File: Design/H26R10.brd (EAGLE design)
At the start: 34.6 x 60 mm, 66 parts, among them P1 HEXABIT_17.32_X2_NO_P5_P10_P1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, U1 STM32F091RBT6STMICROELECTRONI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, U2 AD8275BRMZ, U3 ADR431ARMZ, U4 AD8295BCPZ-WP, U5 AD7687BRMZ, X1 XTALL_CSTCE8M00G52, X2 1751251, X3 CON-PHOENIX-350_1751277

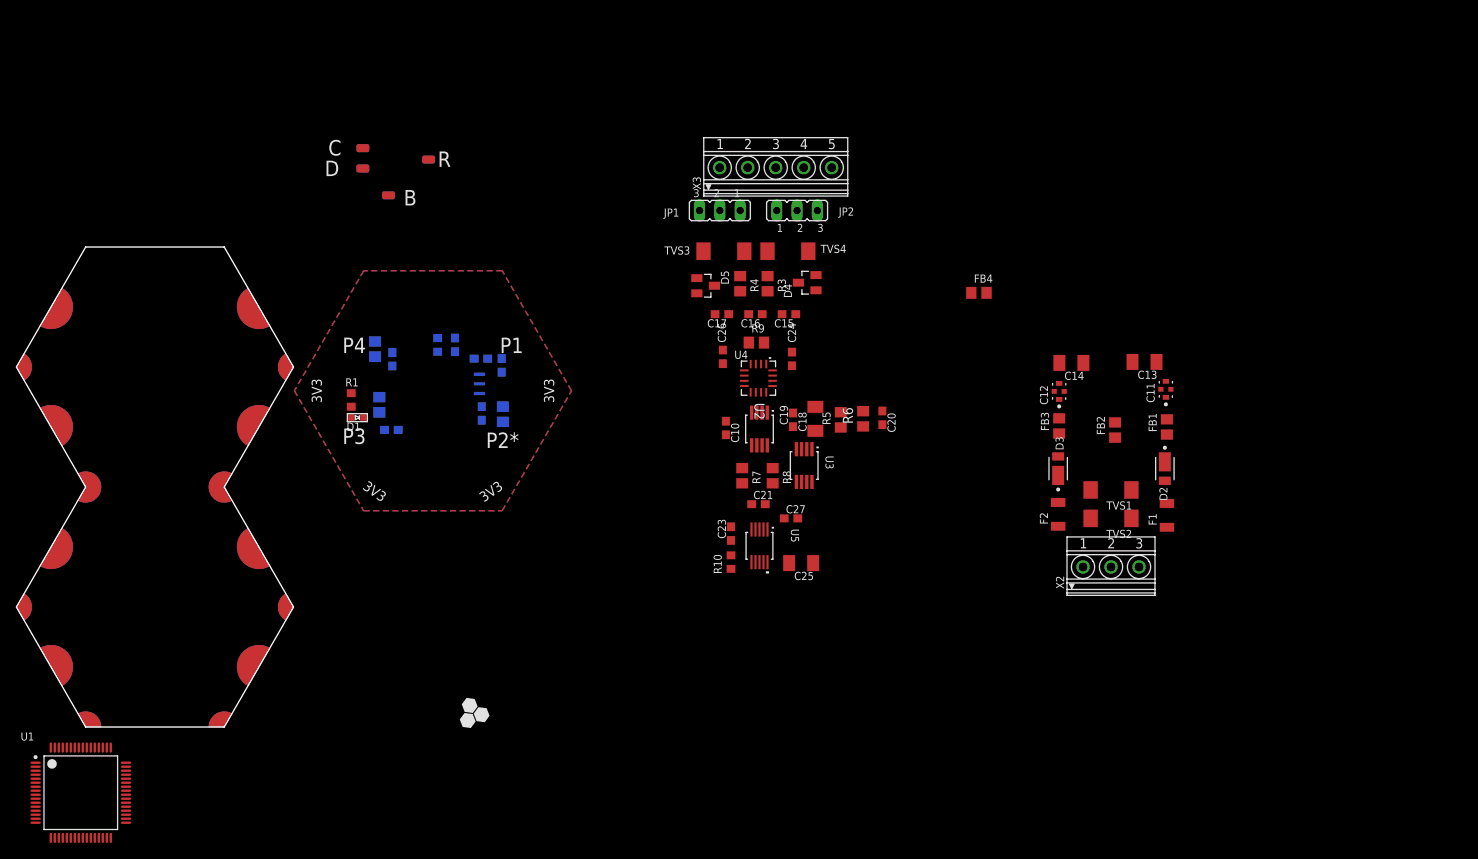
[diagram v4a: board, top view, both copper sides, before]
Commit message: Rearrange uart connections Route analog section
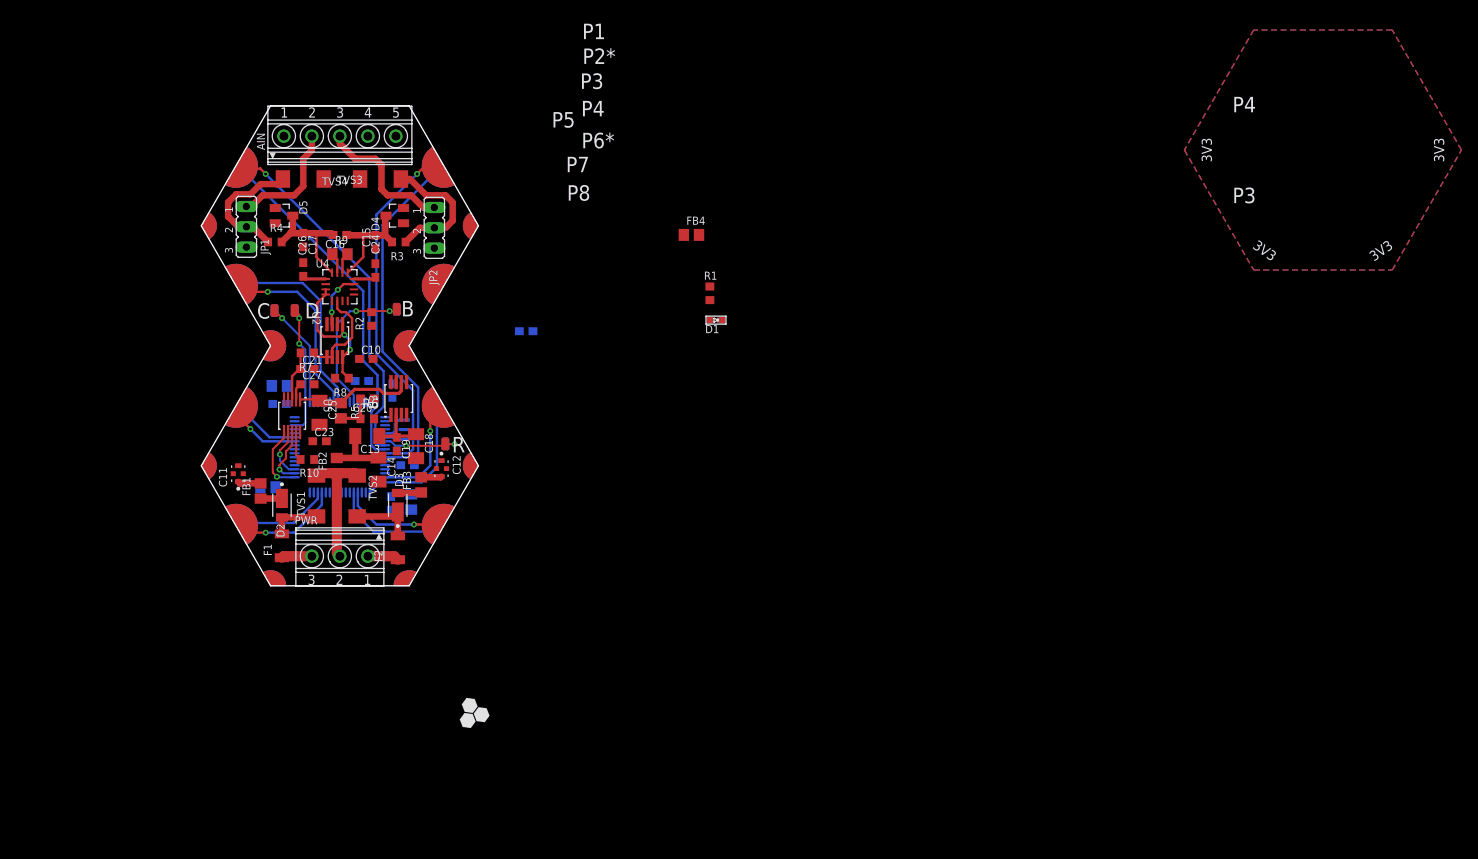
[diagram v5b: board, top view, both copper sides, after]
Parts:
- removed X2: 1751251, con-phoenix-350:1751251
- removed X3: CON-PHOENIX-350_1751277, Hexabitz:CON-PHOENIX-350_1751277
- added AIN: CON-PHOENIX-350_1751277, Hexabitz:CON-PHOENIX-350_1751277
- added PWR: 1751251, con-phoenix-350:1751251
- R3, R4, R6, R7, R8: device Hexabitz:R-0805 -> Hexabitz:R-0603
- moved C11 116.4 mm to (10.3, 24.3)
- moved FB1 113.6 mm to (13.1, 22.1)
- moved F1 110.7 mm to (15.7, 15.2)
- moved D2 110.5 mm to (15.7, 20.3)
- moved TVS1 99.3 mm to (20.1, 21.5), turned to 90 degrees
- moved C13 97.6 mm to (26.4, 29.0)
- moved FB2 97.4 mm to (22.6, 25.3)
- moved TVS2 94.3 mm to (25.1, 21.5), turned to 270 degrees
- moved C14 87.6 mm to (27.8, 24.8), turned to 270 degrees
- moved D3 82.7 mm to (30.2, 20.3)
- moved F2 82.7 mm to (30.2, 15.0)
- moved FB3 80.1 mm to (33.1, 22.9)
- moved C12 77.8 mm to (35.7, 24.9), turned to 270 degrees
- moved C20 64.4 mm to (26.4, 33.7), turned to 180 degrees
- moved C25 63.1 mm to (20.4, 31.9), turned to 270 degrees
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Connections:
- net +5V renamed +2.5V
- removed net N$29: P1.PAD_PU1
- removed net N$30: P1.PAD_PU2
- removed net N$34: P1.PAD_PD1, P1.PAD_PD2, P1.PAD_PD3, P1.PAD_PD4, P1.PAD_PD6, P1.PAD_PD7, P1.PAD_PD8, P1.PAD_PD9, P1.PAD_PU3, P1.PAD_PU4, P1.PAD_PU6, P1.PAD_PU7, P1.PAD_PU8, P1.PAD_PU9
- removed net UART1_RX: U1.43
- removed net UART1_TX: U1.42
- new net UART1_RX*: P1.PAD_PD7, U1.43
- new net UART1_TX*: P1.PAD_PU7, U1.42
- net +15V: now also AIN.5; no longer X3.5
- net -15V: now also AIN.4; no longer X3.4
- net AGND: now also AIN.1; no longer X3.1
- net N$1: now also AIN.3; no longer X3.3
- net N$15: now also PWR.3; no longer X2.3
- net N$16: now also PWR.1; no longer X2.1
- net N$19: now also PWR.2; no longer X2.2
- net N$2: now also AIN.2; no longer X3.2
- net UART2_RX*: now also P1.PAD_PD3
- net UART2_TX*: now also P1.PAD_PU3
- net UART3_RX: now also P1.PAD_PD6
- net UART3_TX: now also P1.PAD_PU6
- net UART4_RX: now also P1.PAD_PD2
- net UART4_TX: now also P1.PAD_PU2
- net UART5_RX: now also P1.PAD_PD8
- net UART5_TX: now also P1.PAD_PU8
- net UART6_RX: now also P1.PAD_PD4
- net UART6_TX: now also P1.PAD_PU4
- net UART7_RX: now also P1.PAD_PD9
- net UART7_TX: now also P1.PAD_PU9
- net UART8_RX: now also P1.PAD_PD1
- net UART8_TX: now also P1.PAD_PU1
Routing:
- net UART8_TX: track 0.00 -> 45.1 mm, vias 0 -> 1
- net UART7_TX: track 0.00 -> 44.9 mm, vias 0 -> 1
- net UART8_RX: track 0.00 -> 44.6 mm
- net UART7_RX: track 0.00 -> 43.9 mm
- net UART5_RX: track 0.00 -> 24.4 mm
- net UART5_TX: track 0.00 -> 23.2 mm, vias 0 -> 1
- net B1: track 0.00 -> 19.9 mm, vias 0 -> 2
- net N$1: track 0.00 -> 17.8 mm
- net N$7: track 0.00 -> 17.2 mm, vias 0 -> 2
- net UART2_RX*: track 0.00 -> 17.1 mm
- net AD8295_A1O: track 0.00 -> 17.1 mm, vias 0 -> 2
- net N$8: track 0.00 -> 16.9 mm
- net N$10: track 0.00 -> 16.1 mm
- net N$19: track 0.00 -> 15.9 mm
- net N$12: track 0.00 -> 15.0 mm
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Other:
- board text added: "P5"
- board text added: "P6*"
- board text added: "P7"
- board text added: "P8"

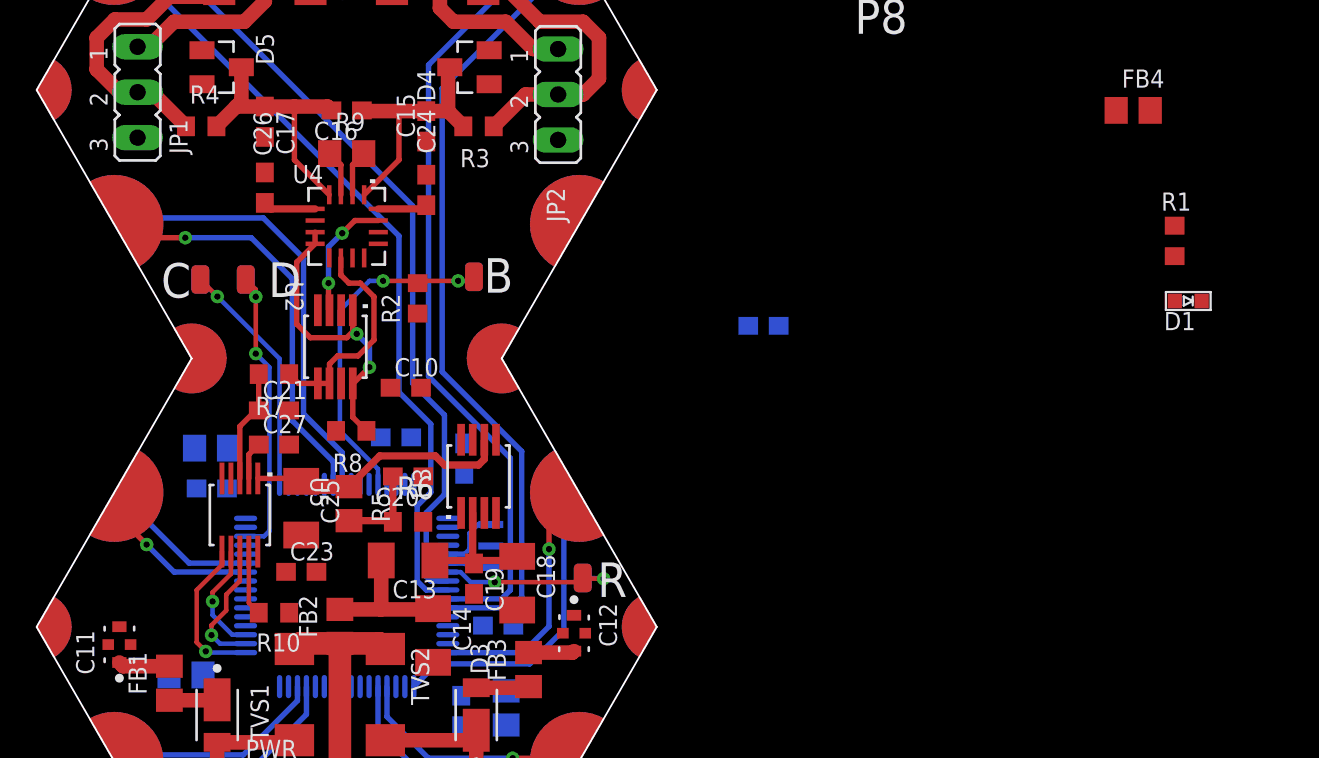
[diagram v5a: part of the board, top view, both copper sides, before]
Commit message: More routing Add 2 more layers Add layer stack note
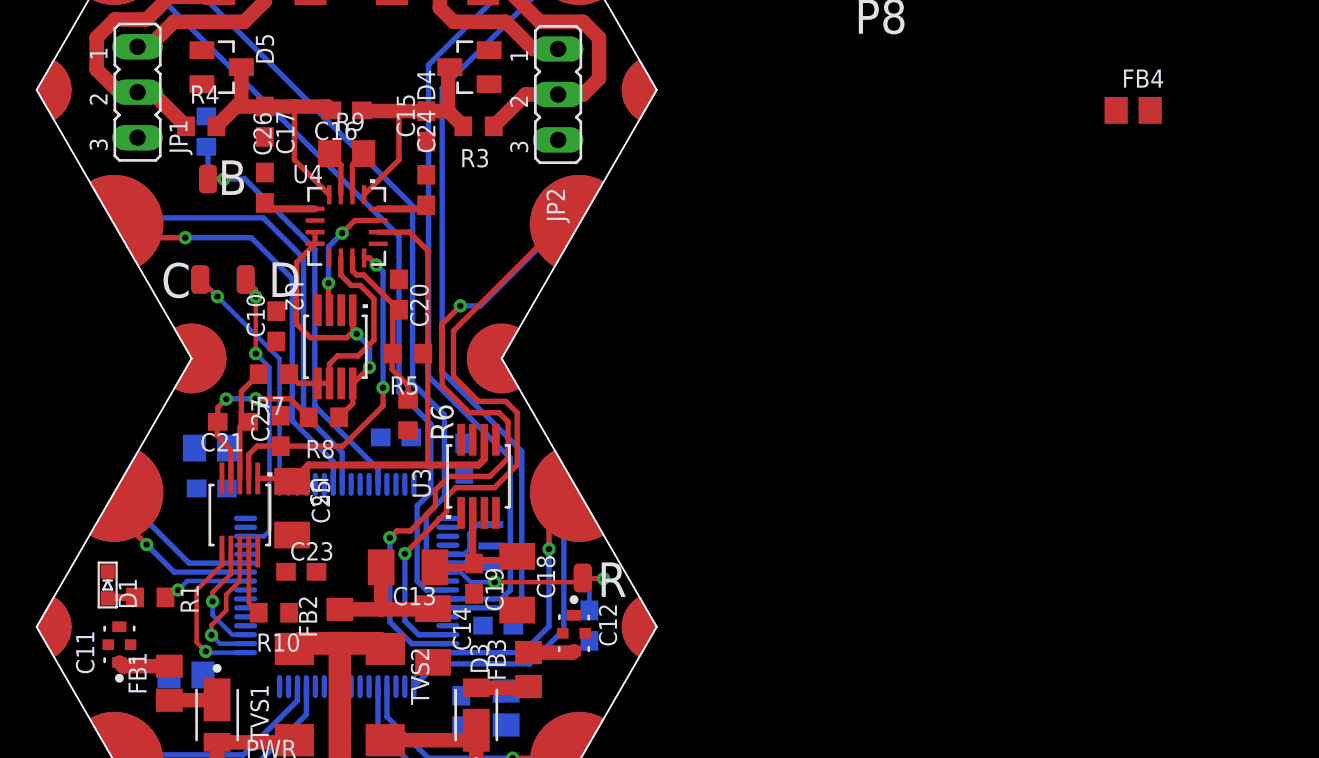
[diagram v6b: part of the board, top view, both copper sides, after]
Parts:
- R5: device Hexabitz:R-0805 -> Hexabitz:R-0603
- moved D1 62.4 mm to (9.63, 27.6), turned to 180 degrees
- moved R1 60.6 mm to (12.0, 26.9), turned to 0 degrees
- moved C8 19.4 mm to (36.5, 25.3), turned to 270 degrees
- moved B 15.8 mm to (15.2, 50.3)
- moved R2 15.0 mm to (15.1, 52.9), flipped to the bottom, turned to 270 degrees
- moved C20 10.2 mm to (25.9, 43.8), turned to 270 degrees
- moved R5 9.01 mm to (26.4, 40.5), turned to 180 degrees
- moved C10 8.01 mm to (19.1, 42.0), turned to 90 degrees
- moved R6 5.97 mm to (26.4, 37.1), turned to 270 degrees
- moved C21 2.37 mm to (16.6, 36.7), turned to 180 degrees
- moved R8 1.70 mm to (21.7, 37.0)
- moved C27 0.85 mm to (19.3, 36.2), turned to 90 degrees
- moved C25 0.51 mm to (19.9, 31.9)
- moved C13 0.38 mm to (26.4, 28.6)
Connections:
- net N$3: now also U1.41; no longer U1.44
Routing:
- net UART4_RX: track 0.00 -> 36.9 mm, vias 0 -> 2
- net UART4_TX: track 0.00 -> 34.2 mm, vias 0 -> 1
- net AD8295_A2O: track 2.12 -> 18.8 mm, vias 0 -> 2
- net +2.5V: track 15.0 -> 30.0 mm
- net N$28: track 0.00 -> 10.0 mm, vias 0 -> 2
- net B1: track 19.9 -> 25.6 mm, vias 2 -> 1
- net N$3: track 0.00 -> 4.85 mm, vias 0 -> 1
- net N$25: track 5.02 -> 9.60 mm
- net R1: track 10.2 -> 12.2 mm
- net N$4: track 0.00 -> 1.55 mm
- net AD8295_A1O: track 17.1 -> 16.3 mm
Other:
- board text added: "Total Thickness 1.6 mm --------------------------------------------------------- copper_top_l1.gbr : Top Conductor - Copper: Thickness 0.035 mm Dielectric - FR-4: Thickness 0.175 mm copper_inner_l2.gbr : GND Plane - Copper: Thickness 0.035 mm Dielectric - FR-4: Thickness 1.11 mm copper_inner_l3.gbr : VDD Plane - Copper: Thickness 0.035 mm Dielectric - FR-4: Thickness 0.175 mm copper_bottom_l4.gbr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"

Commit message: Finished routing Added polygons
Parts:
- moved FB4 62.3 mm to (13.5, 22.1), flipped to the bottom, turned to 90 degrees
- moved C10 7.16 mm to (24.8, 37.7), turned to 270 degrees
- moved C7 2.88 mm to (16.4, 21.0), turned to 270 degrees
- moved D5 2.43 mm to (18.4, 56.8), turned to 90 degrees
- moved D4 2.30 mm to (27.6, 56.8), turned to 270 degrees
- moved C12 2.16 mm to (35.6, 22.7), turned to 90 degrees
- moved R6 1.05 mm to (26.7, 38.1)
- moved C6 0.52 mm to (25.9, 35.3)
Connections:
- removed net N$24: C13.2, C14.1, FB2.2
- net AGND: now also C11.2, C11.2-2, C12.2, C12.2-2, C13.2, C14.1, FB2.2
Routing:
- net VDD: track 0.00 -> 192.2 mm, vias 0 -> 16
- net +15V: track 10.5 -> 90.1 mm, vias 0 -> 5
- net -15V: track 2.95 -> 59.6 mm, vias 0 -> 5
- net AGND: track 0.00 -> 41.3 mm, vias 0 -> 7
- net N$24: track 7.59 -> 0.00 mm
- net AD8295_A1O: track 16.3 -> 19.0 mm
- net UART4_TX: track 34.2 -> 35.4 mm
- net N$25: track 9.60 -> 8.69 mm
- net UART4_RX: track 36.9 -> 37.7 mm
- added copper zone on layer 1, net AGND
- added copper zone on layer 2, net AGND
- added copper zone on layer 15, net GND

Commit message: arrange top silkscreen
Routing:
- net -15V: track 59.6 -> 69.5 mm
- net AGND: vias 7 -> 18
